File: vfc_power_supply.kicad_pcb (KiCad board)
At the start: 4 copper layers, 65 x 56 mm, 49 parts, among them J1 Connector_RJ45_Magjack_Abraco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, J2 Connector_RJ45_Magjack_Abraco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, J3 Conn_01x03_Male, P1 Conn_02x20_Odd_Even, U1 LT8653S, U2 LT8636, U3 LTC2497

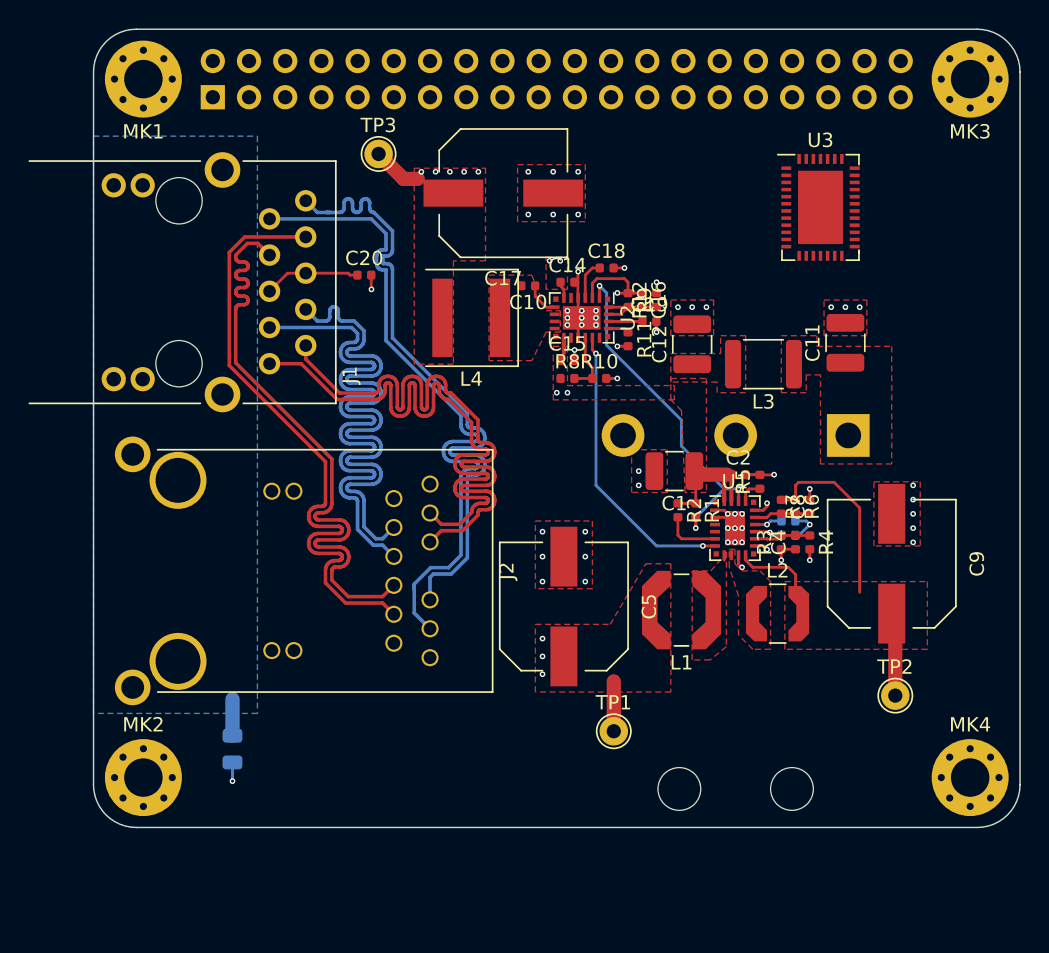
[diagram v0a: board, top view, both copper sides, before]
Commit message: nearly done, just missing output protection
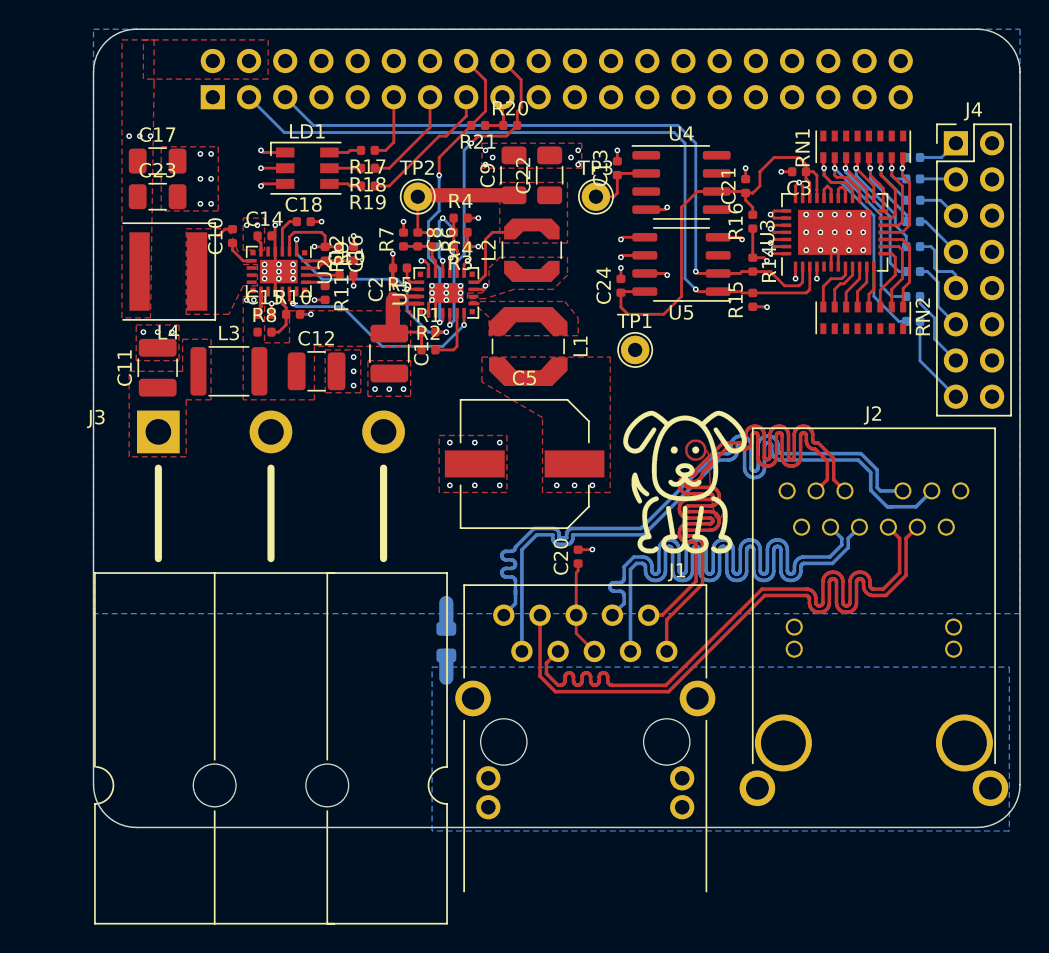
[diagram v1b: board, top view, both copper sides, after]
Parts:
- removed MK1, MK2, MK4: M2.5, MountingHole:MountingHole_2.7mm_M2.5_Pad_Via
- removed MK3: M2.5, MountingHole:MountingHole_2.7mm_Pad_Via
- added C13: 1u, Capacitor_SMD:C_0402_1005Metric, F.Cu at (236.8, 103.8)
- added C21: 1u, Capacitor_SMD:C_0402_1005Metric, F.Cu at (245.8, 105.0)
- added C22: 47u, Capacitor_SMD:C_1206_3216Metric, F.Cu at (232.0, 104.2)
- added C23: 47u, Capacitor_SMD:C_1206_3216Metric, F.Cu at (204.5, 105.8)
- added C24: 100n, Capacitor_SMD:C_0402_1005Metric, F.Cu at (237.0, 112.0)
- added C3: 100n, Capacitor_SMD:C_0402_1005Metric, F.Cu at (249.5, 104.0)
- added J4: Conn_02x08_Odd_Even, Connector_PinHeader_2.54mm:PinHeader_2x08_P2.54mm_Vertical, F.Cu at (260.5, 102.0)
- added LD1: LED_Cree_CLX6E-FKC, LED_SMD:LED_RGB_PLCC-6, F.Cu at (215.0, 103.8)
- added M1: Logo_10mmx10mm, Misc_WUT:Logo_10mmx10mm_Monocle, F.Cu at (241.5, 125.8)
- added R14: DNF, Resistor_SMD:R_0402_1005Metric, F.Cu at (246.2, 110.5)
- added R15: DNF, Resistor_SMD:R_0402_1005Metric, F.Cu at (246.2, 113.0)
- added R16: DNF, Resistor_SMD:R_0402_1005Metric, F.Cu at (246.2, 107.5)
- added R17: 7k5, Resistor_SMD:R_0402_1005Metric, F.Cu at (219.2, 102.5)
- added R18: 33k, Resistor_SMD:R_0402_1005Metric, F.Cu at (219.2, 103.8)
- added R19: 22k, Resistor_SMD:R_0402_1005Metric, F.Cu at (219.2, 105.0)
- added R20: 10k, Resistor_SMD:R_0402_1005Metric, F.Cu at (229.2, 100.8)
- added R21: 10k, Resistor_SMD:R_0402_1005Metric, F.Cu at (227.0, 100.8)
- added R22: R, Resistor_SMD:R_0402_1005Metric, B.Cu at (257.5, 103.0)
- added R23: R, Resistor_SMD:R_0402_1005Metric, B.Cu at (257.5, 104.5)
- added R24: R, Resistor_SMD:R_0402_1005Metric, B.Cu at (257.5, 106.0)
- added R25: R, Resistor_SMD:R_0402_1005Metric, B.Cu at (257.5, 107.5)
- added R26: R, Resistor_SMD:R_0402_1005Metric, B.Cu at (257.5, 109.2)
- added R27: R, Resistor_SMD:R_0402_1005Metric, B.Cu at (257.5, 111.0)
- added R28: R, Resistor_SMD:R_0402_1005Metric, B.Cu at (257.5, 112.8)
- added R29: R, Resistor_SMD:R_0402_1005Metric, B.Cu at (257.5, 114.5)
- added RN1: 10k, Resistor_SMD:R_Cat16-8, F.Cu at (254.0, 102.2)
- added RN2: 10k, Resistor_SMD:R_Cat16-8, F.Cu at (254.0, 114.2)
- added U4: REF5030ID, Package_SO:SOIC-8_3.9x4.9mm_P1.27mm, F.Cu at (241.2, 104.8)
- added U5: PCT2075D, Package_SO:SO-8_3.9x4.9mm_P1.27mm, F.Cu at (241.2, 110.5)
- C17, C9: value 100u -> 47u; footprint Capacitor_WUT:Wurth_WCAP_PSHP -> Capacitor_SMD:C_1206_3216Metric
- J3: moved to F.Cu
- moved J2 54.2 mm to (254.8, 147.2), turned to 0 degrees
- moved TP2 48.4 mm to (222.8, 105.8)
- moved C11 48.3 mm to (204.5, 117.8)
- moved J1 43.0 mm to (234.5, 144.0), turned to 0 degrees
- moved J3 40.5 mm to (208.5, 122.2), turned to 180 degrees
- moved C9 38.0 mm to (229.5, 104.2), turned to 90 degrees
- moved L3 37.5 mm to (209.5, 118.0), turned to 0 degrees
- moved R7 34.1 mm to (221.8, 108.8)
- moved R4 33.4 mm to (225.8, 107.2), turned to 0 degrees
- moved C4 32.0 mm to (225.8, 108.2), turned to 180 degrees
- moved C8 31.7 mm to (222.8, 108.8)
- moved R6 31.7 mm to (223.8, 108.8)
- moved C7 31.5 mm to (224.2, 108.8), turned to 90 degrees
- moved C6 31.3 mm to (225.2, 108.8), turned to 90 degrees
- moved L2 30.8 mm to (230.8, 109.5), turned to 90 degrees
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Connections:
- P1 pad 1: +3V3 -> Net-(P1-Pad1)
- P1 pad 17: Net-(P1-Pad17) -> +3V3
- U1 pad 3: Net-(U1-Pad3) -> /GPIO23(GEN4)
- U1 pad 4: Net-(U1-Pad4) -> /GPIO24(GEN5)
- U3 pad 10: Net-(U3-Pad10) -> /ADC/CH2
- U3 pad 11: Net-(U3-Pad11) -> /ADC/CH3
- U3 pad 12: Net-(U3-Pad12) -> /ADC/CH4
- U3 pad 13: Net-(U3-Pad13) -> /ADC/CH5
- U3 pad 14: Net-(U3-Pad14) -> /ADC/CH6
- U3 pad 15: Net-(U3-Pad15) -> /ADC/CH7
- U3 pad 16: Net-(U3-Pad16) -> /ADC/CH8
- U3 pad 17: Net-(U3-Pad17) -> /ADC/CH9
- U3 pad 18: Net-(U3-Pad18) -> /ADC/CH10
- U3 pad 19: Net-(U3-Pad19) -> /ADC/CH11
- U3 pad 2: Net-(U3-Pad2) -> /GPIO3(SCL1)
- U3 pad 20: Net-(U3-Pad20) -> /ADC/CH12
- U3 pad 21: Net-(U3-Pad21) -> /ADC/CH13
- U3 pad 22: Net-(U3-Pad22) -> /ADC/CH14
- U3 pad 23: Net-(U3-Pad23) -> /ADC/CH15
- U3 pad 28: Net-(U3-Pad28) -> VDDA
- U3 pad 29: Net-(U3-Pad29) -> VDDA
- U3 pad 3: Net-(U3-Pad3) -> /GPIO2(SDA1)
- U3 pad 30: Net-(U3-Pad30) -> GND
- U3 pad 35: Net-(U3-Pad35) -> GND
- U3 pad 36: Net-(U3-Pad36) -> GND
- U3 pad 37: Net-(U3-Pad37) -> GND
- U3 pad 38: Net-(U3-Pad38) -> GND
- U3 pad 7: Net-(U3-Pad7) -> GND
- U3 pad 8: Net-(U3-Pad8) -> /ADC/CH0
- U3 pad 9: Net-(U3-Pad9) -> /ADC/CH1
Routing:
- net /GPIO2(SDA1): track 0.00 -> 52.3 mm, vias 0 -> 1
- net /GPIO3(SCL1): track 0.00 -> 48.4 mm, vias 0 -> 1
- net +3V3: track 0.00 -> 39.2 mm, vias 0 -> 2
- net GND: track 22.6 -> 57.2 mm, vias 56 -> 91
- net VDDA: track 0.00 -> 32.0 mm
- net /GPIO24(GEN5): track 0.00 -> 23.4 mm, vias 0 -> 2
- net /GPIO23(GEN4): track 0.00 -> 22.0 mm, vias 0 -> 2
- net /ADC/CH15: track 0.00 -> 18.1 mm, vias 0 -> 1
- net /ADC/CH14: track 0.00 -> 15.7 mm, vias 0 -> 1
- net +5V: track 24.6 -> 11.3 mm, vias 6 -> 4
- net /ADC/CH13: track 0.00 -> 12.8 mm, vias 0 -> 1
- net /ADC/CH12: track 0.00 -> 10.4 mm, vias 0 -> 1
- net /GPIO22(GEN3): track 0.00 -> 9.77 mm
- net /ADC/CH11: track 0.00 -> 8.95 mm, vias 0 -> 1
- net +12V: track 26.3 -> 17.5 mm
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- added copper zone on B.Cu, net GND
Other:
- net class Ethernet: clearance 0.16 -> 0.5

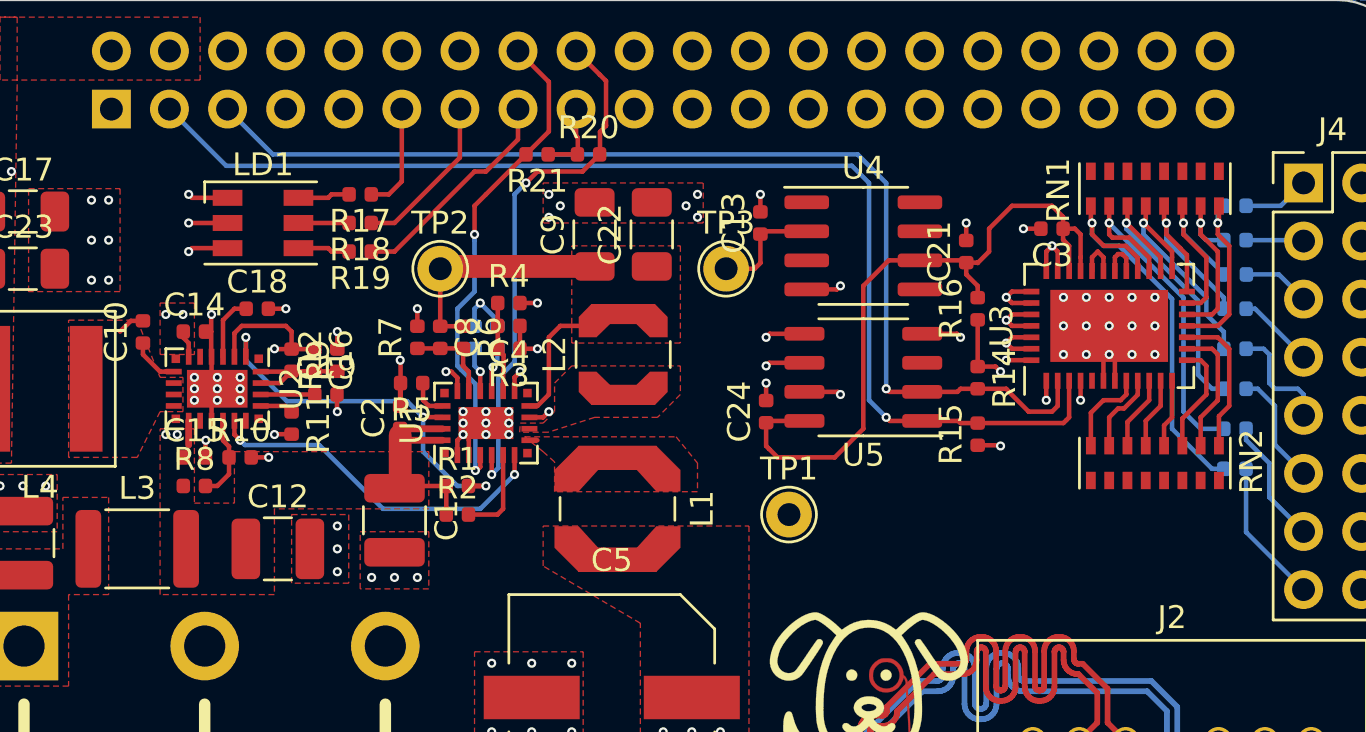
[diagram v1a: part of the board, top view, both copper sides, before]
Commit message: Added notes to schematic
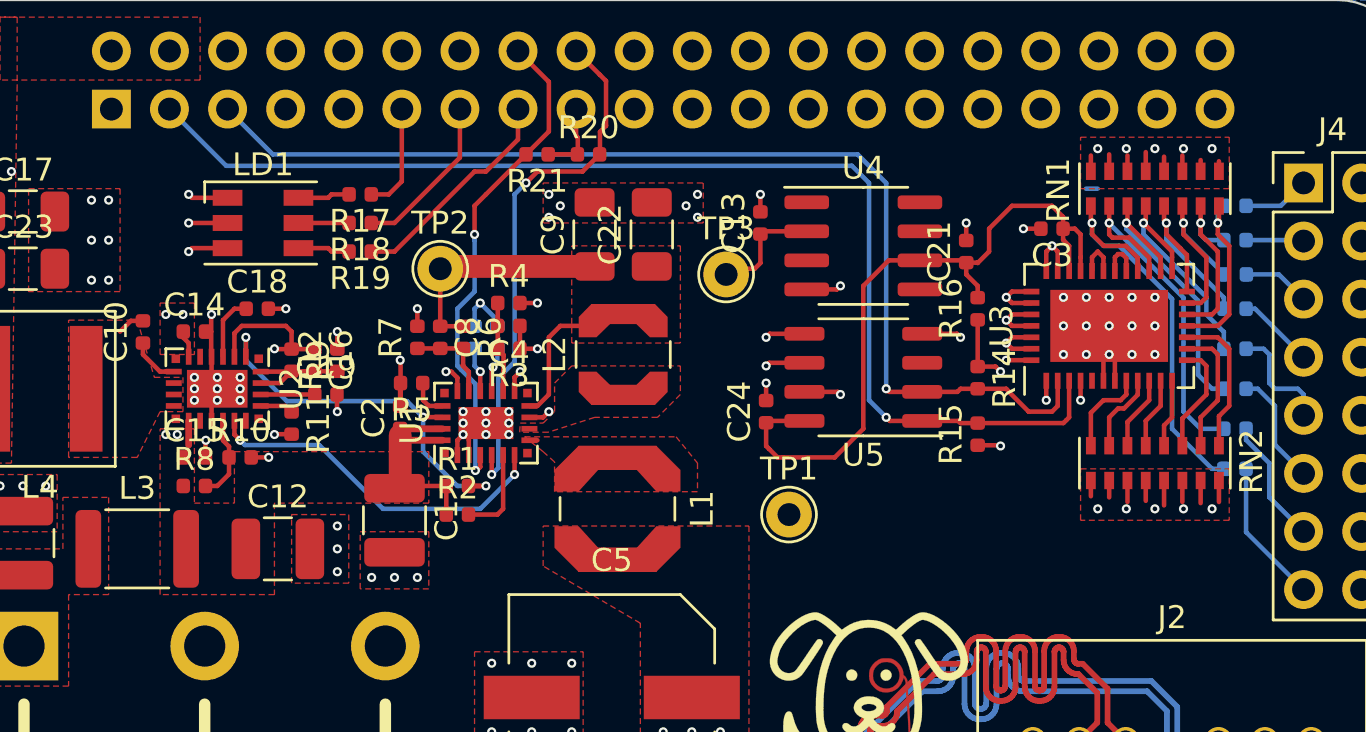
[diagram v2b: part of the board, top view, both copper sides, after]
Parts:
- moved TP3 0.25 mm to (235.2, 106.0)
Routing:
- net GND: track 57.2 -> 71.6 mm, vias 91 -> 101
- net +5V: track 11.3 -> 12.8 mm
- net (no net): track 0.00 -> 0.51 mm
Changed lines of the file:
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@@
     (thickness 1.6)
     (drawings 23)
-    (tracks 1943)
+    (tracks 1971)
     (zones 0)
     (modules 74)
@@
   )
   (setup
-    (last_trace_width 0.2)
+    (last_trace_width 1)
     (user_trace_width 0.3)
     (user_trace_width 1)
@@
   )
   (module TestPoint:TestPoint_THTPad_D2.0mm_Drill1.0mm (layer F.Cu)
-    (at 235.25 105.75)
+    (at 235.25 106)
     (descr "THT pad as test Point, diameter 2.0mm, hole diameter 1.0mm")
     (tags "test point THT pad")
@@
     (effects (font (size 2 1.7) (thickness 0.12)) (justify left))
   )
+  (via (at 255.25 100.5) (size 0.4) (drill 0.2) (layers F.Cu B.Cu) (net 3))
+  (via (at 251.5 100.5) (size 0.4) (drill 0.2) (layers F.Cu B.Cu) (net 3))
+  (via (at 254 100.5) (size 0.4) (drill 0.2) (layers F.Cu B.Cu) (net 3))
+  (via (at 252.75 100.5) (size 0.4) (drill 0.2) (layers F.Cu B.Cu) (net 3))
+  (via (at 256.5 100.5) (size 0.4) (drill 0.2) (layers F.Cu B.Cu) (net 3))
+  (segment (start 251.2 101.74) (end 251.2 100.8) (width 0.2) (layer F.Cu) (net 3))
+  (segment (start 256.8 101.74) (end 256.8 101.05) (width 0.2) (layer F.Cu) (net 3))
+  (segment (start 255.2 101.74) (end 255.2 100.8) (width 0.2) (layer F.Cu) (net 3))
+  (segment (start 256 101.74) (end 256 101) (width 0.2) (layer F.Cu) (net 3))
+  (segment (start 252 101.74) (end 252 100.75) (width 0.2) (layer F.Cu) (net 3))
+  (segment (start 253.6 101.74) (end 253.6 100.65) (width 0.2) (layer F.Cu) (net 3))
+  (segment (start 254.4 101.74) (end 254.4 100.85) (width 0.2) (layer F.Cu) (net 3))
+  (segment (start 252.8 101.74) (end 252.8 100.8) (width 0.2) (layer F.Cu) (net 3))
+  (segment (start 250.985 102.25) (end 251.5 102.25) (width 0.2) (layer B.Cu) (net 0))
   (via (at 247.25 113.5) (size 0.4) (drill 0.2) (layers F.Cu B.Cu) (net 1))
   (segment (start 246.25 113.47) (end 247.22 113.47) (width 0.2) (layer F.Cu) (net 1))
@@
   (via (at 203.25 101.5) (size 0.4) (drill 0.2) (layers F.Cu B.Cu) (net 2))
   (via (at 204 101.5) (size 0.4) (drill 0.2) (layers F.Cu B.Cu) (net 2))
+  (segment (start 235.25 106) (end 235.25 104.5) (width 1) (layer In2.Cu) (net 2))
   (via (at 208.25 106.25) (size 0.4) (drill 0.2) (layers F.Cu B.Cu) (net 3))
   (via (at 208.25 102.75) (size 0.4) (drill 0.2) (layers F.Cu B.Cu) (net 3))
@@
   (segment (start 252.25 108.5) (end 252 108.25) (width 0.2) (layer F.Cu) (net 3))
   (segment (start 252.25 110.65) (end 252.25 108.5) (width 0.2) (layer F.Cu) (net 3))
+  (segment (start 251.2 115.01) (end 251.2 115.7) (width 0.2) (layer F.Cu) (net 3))
+  (segment (start 252 115.01) (end 252 115.75) (width 0.2) (layer F.Cu) (net 3))
+  (segment (start 252.8 115.01) (end 252.8 115.95) (width 0.2) (layer F.Cu) (net 3))
+  (segment (start 253.6 115.01) (end 253.6 115.9) (width 0.2) (layer F.Cu) (net 3))
+  (segment (start 254.4 115.01) (end 254.4 116.1) (width 0.2) (layer F.Cu) (net 3))
+  (segment (start 255.2 115.01) (end 255.2 115.95) (width 0.2) (layer F.Cu) (net 3))
+  (segment (start 256 115.01) (end 256 116) (width 0.2) (layer F.Cu) (net 3))
+  (segment (start 256.8 115.01) (end 256.8 115.95) (width 0.2) (layer F.Cu) (net 3))
+  (via (at 251.5 116.25) (size 0.4) (drill 0.2) (layers F.Cu B.Cu) (net 3))
+  (via (at 252.75 116.25) (size 0.4) (drill 0.2) (layers F.Cu B.Cu) (net 3))
+  (via (at 254 116.25) (size 0.4) (drill 0.2) (layers F.Cu B.Cu) (net 3))
+  (via (at 255.25 116.25) (size 0.4) (drill 0.2) (layers F.Cu B.Cu) (net 3))
+  (via (at 256.5 116.25) (size 0.4) (drill 0.2) (layers F.Cu B.Cu) (net 3))
   (segment (start 250.25 112.25) (end 250.25 110.65) (width 0.2) (layer F.Cu) (net 9))
   (segment (start 243.825 112.405) (end 245.405 112.405) (width 0.2) (layer F.Cu) (net 9))
@@
       (pts
         (xy 210.5 112) (xy 209.5 114) (xy 206.5 114) (xy 206.5 108) (xy 209.5 108)
-        (xy 210.5 110.5) (xy 211.5 110.5) (xy 211.5 112)
+        (xy 210.25 110.5) (xy 211.5 110.5) (xy 211.5 112)
       )
     )
@@
     (polygon
       (pts
-        (xy 212 116) (xy 213.75 116) (xy 213.75 113.75) (xy 222.25 113.75) (xy 222.25 116.25)
-        (xy 215.5 116.25) (xy 215.5 120) (xy 210.5 120) (xy 210.5 112.75) (xy 212 112.75)
+        (xy 212 116) (xy 213.75 116) (xy 213.75 113.75) (xy 222.25 113.75) (xy 222.25 116)
+        (xy 215.5 116) (xy 215.5 120) (xy 210.5 120) (xy 210.5 112.75) (xy 212 112.75)
       )
     )
@@
       )
     )
+  )
+  (zone (net 3) (net_name GND) (layer F.Cu) (hatch edge 0.508)
+    (connect_pads (clearance 0.16))
+    (min_thickness 0.254)
+    (fill yes (arc_segments 32) (thermal_gap 0.508) (thermal_bridge_width 0.508))
+    (polygon
+      (pts
+        (xy 257.25 116.75) (xy 250.75 116.75) (xy 250.75 114.5) (xy 257.25 114.5)
+      )
+    )
+  )
+  (zone (net 3) (net_name GND) (layer F.Cu) (hatch edge 0.508)
+    (connect_pads (clearance 0.16))
+    (min_thickness 0.254)
+    (fill yes (arc_segments 32) (thermal_gap 0.508) (thermal_bridge_width 0.508))
+    (polygon
+      (pts
+        (xy 250.75 100) (xy 257.25 100) (xy 257.25 102.25) (xy 250.75 102.25)
+      )
+    )
